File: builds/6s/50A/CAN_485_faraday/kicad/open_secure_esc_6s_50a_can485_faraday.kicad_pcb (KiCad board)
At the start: 4 copper layers, 32 x 66.1 mm, 65 parts, among them J1 SolderPad_1x04_SMD_P1.27mm_Pr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, J2 SolderPad_1x02_SMD_P2.54mm, J3 SolderPad_1x02_SMD_P2.54mm, J4A SolderWirePad_1x01_SMD_5x10mm, J4B SolderWirePad_1x01_SMD_5x10mm, J4C SolderWirePad_1x01_SMD_5x10mm, J5A SolderWire-6sqmm_1x01_D3.5mm_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, J5B SolderWire-6sqmm_1x01_D3.5mm_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, Q1 Toshiba_2-5W1A_SOP-Advance-N_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, Q2 Toshiba_2-5W1A_SOP-Advance-N_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, Q3 Toshiba_2-5W1A_SOP-Advance-N_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, Q4 Toshiba_2-5W1A_SOP-Advance-N_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, Q5 Toshiba_2-5W1A_SOP-Advance-N_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, Q6 Toshiba_2-5W1A_SOP-Advance-N_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, U1 LQFP-64_10x10mm_P0.5mm, U2 Infineon_PG-USON-10-2-4_3x3mm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, U3 SOIC-20W_7.5x12.8mm_P1.27mm, U4 SOIC-20W_7.5x12.8mm_P1.27mm, U5 TI_RTA0040B_WQFN-40_6x6mm_P0.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, U6 SOIC-8_3.9x4.9mm_P1.27mm, U7 SOIC-8_3.9x4.9mm_P1.27mm, U8 SOIC-8_3.9x4.9mm_P1.27mm

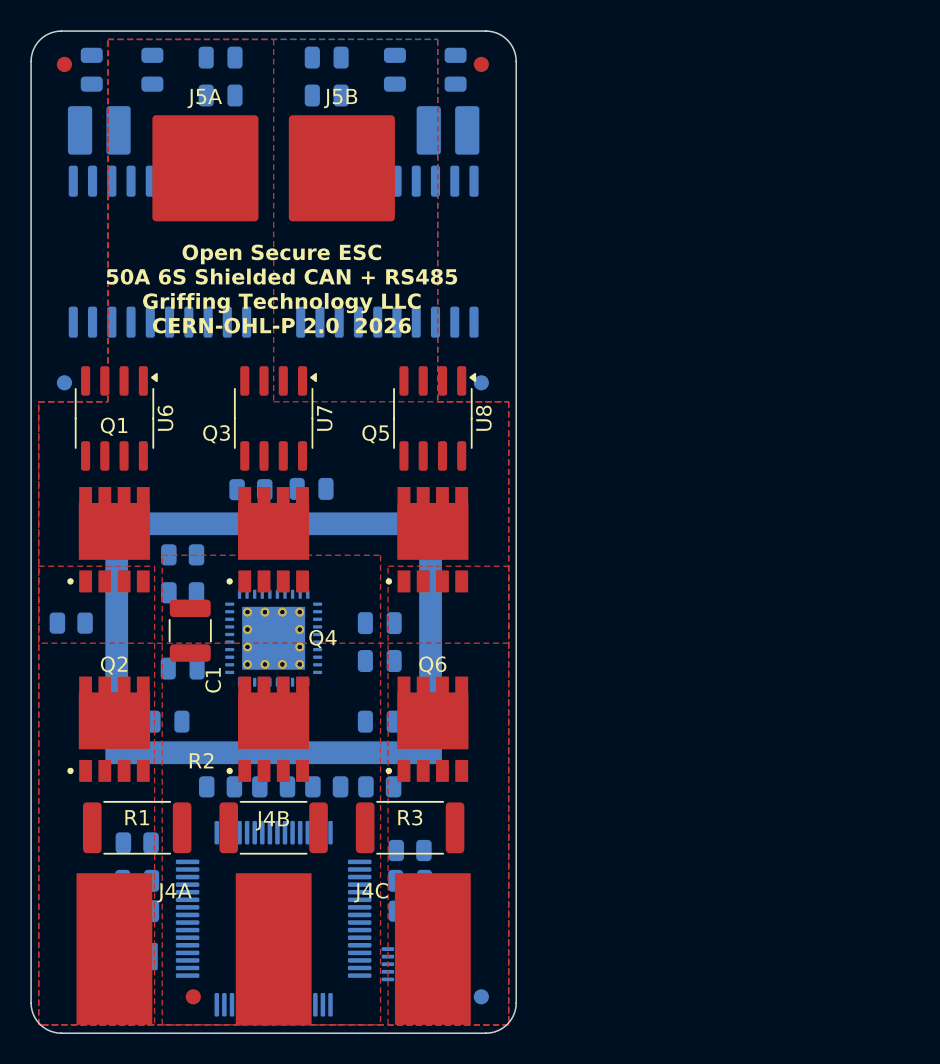
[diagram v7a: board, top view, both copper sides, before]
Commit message: Stage RHB MCU footprint on-canvas; make RHB the standard MCU package
Two pieces of follow-up to the RHB (VQFN-32) MCU package swap:

- Add the new U1 footprint (Package_DFN_QFN:Texas_RHB0032E_VQFN-32-1EP_
  5x5mm) to each affected .kicad_pcb, replacing the stale LQFP-64
  footprint in place. Every pad is wired to its correct net (verified
  against each board's own net table), but the whole footprint is
  staged OFF-BOARD at fixed clear-of-outline coordinates rather than
  auto-placed or dropped into the old LQFP-64's spot, so final position
  is a manual decision. kicad-cli pcb drc re-run on each board: no new
  violation categories, unconnected-item counts unchanged.

  Done for CAN_485_faraday, CAN_485_faraday_sameend, and
  CAN_485_faraday_sameend_faceted. CAN_485_faraday_faceted's .kicad_pcb
  was left untouched -- it's open in a live, running KiCad GUI session
  (lock file + process observed), and writing to it now risks the next
  GUI save silently discarding the change. Tracked in TODO.md 12.5.bg.

- Swap U1 from MSPM0G3518_Q1_PM to MSPM0G3518_Q1_RHB in the
  CAN_485_faraday_sameend schematic too (same technique as the prior
  commit: identical pin coordinates/types/names, only pin numbers
  change, so existing wiring survives). kicad-cli sch erc re-verified
  at 0 errors, same warning set as before the swap.

- Declare RHB the standard MCU package for all builds going forward in
  README.md and both builds' sym-lib-table descriptions, rather than
  treating the first swap as a one-off.

- New open item (TODO.md 12.5.bg.1): the RHB exposed thermal pad (pad
  33) is left without a net in all three staged footprints -- no
  primary-source confirmation was found that it's internally bonded to
  VSS, so it's marked UNVERIFIED per AGENTS.md Sec.1.3 rather than
  assumed.

Co-Authored-By: Claude Sonnet 5 <noreply@anthropic.com>
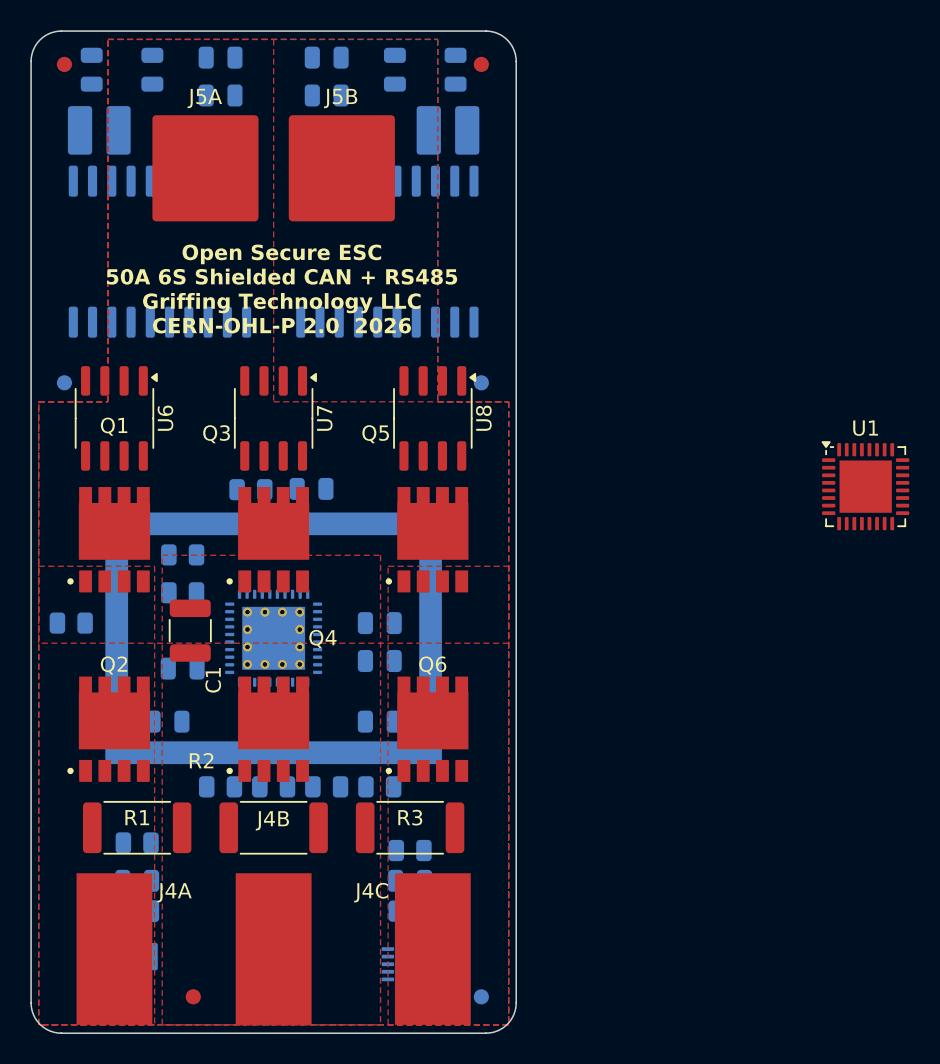
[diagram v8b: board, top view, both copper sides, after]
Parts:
- U1: value LQFP-64_10x10mm_P0.5mm -> MSPM0G3518_Q1_RHB; footprint LQFP-64_10x10mm_P0.5mm -> Package_DFN_QFN:Texas_RHB0032E_VQFN-32-1EP_5x5mm_P0.5mm_EP3.45x3.45mm; moved to F.Cu
- moved U1 48.3 mm to (75.0, 50.0), turned to 0 degrees
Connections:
- U1 pad 1: Net-(U1-GD_SPI_CS) -> Net-(U1-RS485_TXD)
- U1 pad 10: (no net) -> RS485_DE_RE
- U1 pad 12: Net-(J1-Pin_1) -> Net-(U1-PWM_AH)
- U1 pad 13: Net-(J1-Pin_2) -> Net-(U1-PWM_AL)
- U1 pad 14: (no net) -> Net-(U1-PWM_CH)
- U1 pad 15: (no net) -> Net-(U1-PWM_CL)
- U1 pad 16: (no net) -> Net-(U1-CAN_TX)
- U1 pad 17: VBUS_SENSE -> Net-(U1-CAN_RX)
- U1 pad 18: (no net) -> SE_RST
- U1 pad 19: (no net) -> SE_I2C_SCL
- U1 pad 2: GD_SPI_MISO -> Net-(U1-RS485_RXD)
- U1 pad 20: (no net) -> GD_SPI_MISO
- U1 pad 21: (no net) -> Net-(U1-GD_SPI_SCK)
- U1 pad 22: (no net) -> Net-(U1-GD_SPI_MOSI)
- U1 pad 23: (no net) -> Net-(J1-Pin_1)
- U1 pad 24: ADC_IV -> Net-(J1-Pin_2)
- U1 pad 25: ADC_IU -> VBUS_SENSE
- U1 pad 26: ADC_IW -> (no net)
- U1 pad 27: (no net) -> ADC_IV
- U1 pad 28: (no net) -> ADC_IU
- U1 pad 29: (no net) -> ADC_IW
- U1 pad 3: Net-(U1-GD_SPI_MOSI) -> NRST
- U1 pad 30: Net-(U1-CAN_TX) -> (no net)
- U1 pad 31: Net-(U1-CAN_RX) -> (no net)
- U1 pad 33: Net-(U1-RS485_TXD) -> (no net)
- U1 pad 4: Net-(U1-GD_SPI_SCK) -> 3V3
- U1 pad 5: (no net) -> GND
- U1 pad 6: (no net) -> Net-(U1-GD_SPI_CS)
- U1 pad 7: SE_RST -> Net-(U1-PWM_BH)
- U1 pad 8: SE_I2C_SCL -> Net-(U1-PWM_BL)
